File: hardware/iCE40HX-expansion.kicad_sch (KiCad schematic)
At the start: 32 parts, among them J1 EXT3, J2 EXT1, J3 AudioJack3_Ground, J4 Conn_01x34, J5 AudioJack3_Ground, J6 Conn_01x04, J8 DE15_Plug_HighDensity, U1 ADV7180BCP32Z-RL, U2 AMS1117-1.8, Y1 28.63636MHz

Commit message: finished component placement
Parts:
- added C24, C26: 0.1uf, Capacitor_SMD:C_0603_1608Metric, symbol Device:C_Small
- added C25, C27: 10uf, Capacitor_SMD:C_0805_2012Metric, symbol Device:C_Small
- added R56, R57: 270, Resistor_SMD:R_0603_1608Metric, symbol Device:R_Small
- added U5: 74LVC245A, Package_SO:TSSOP-20_4.4x6.5mm_P0.65mm, symbol New_Library:74LVC245A
- C22, C23: footprint Capacitor_SMD:C_0603_1608Metric -> Capacitor_SMD:C_0805_2012Metric
- J3, J5: value AudioJack3_Ground -> ~
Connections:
- net CLK is gone; now on net PIO1_20: J4.2 (Pin_2)
- net EN is gone; now on net PIO1_19: J4.4 (Pin_4)
- net HS is gone; now on net PIO0_20: U1.1 (HS)
- net INTRQ is gone; now on net PIO0_17: U1.32 (~{INTRQ})
- net LLC is gone; now on net PIO0_21: U1.11 (LLC)
- net SFL is gone; now on net PIO0_18: U1.4 (SFL)
- net VS is gone; now on net PIO0_19: U1.31 (VS/FIELD)
- net +1V8: now also U2.2 (VO), C24.1, C25.1
- net +3V3: now also U2.3 (VI), C26.1, C27.1, U5.1 (DIR), U5.19 (OE), U5.20 (VCC)
- net GND: now also U2.1 (GND), C24.2, C25.2, C26.2, C27.2, U5.10 (GND)
- net PIO0_00: no longer J4.29 (Pin_29)
- net PIO0_01: no longer J4.28 (Pin_28)
- net PIO0_02: no longer J4.27 (Pin_27)
- net PIO0_03: no longer J4.26 (Pin_26)
- net PIO0_04: no longer J4.25 (Pin_25)
- net PIO0_05: no longer J4.24 (Pin_24)
- net PIO0_06: no longer J4.23 (Pin_23)
- net PIO0_07: no longer J4.22 (Pin_22)
- net PIO0_08: no longer J4.21 (Pin_21)
- net PIO0_09: now also U1.16 (P0); no longer J4.20 (Pin_20)
- net PIO0_10: now also U1.15 (P1); no longer J4.19 (Pin_19)
- net PIO0_11: now also U1.10 (P2); no longer J4.18 (Pin_18)
- net PIO0_12: now also U1.9 (P3); no longer J4.17 (Pin_17)
- net PIO0_13: now also U1.8 (P4); no longer J4.16 (Pin_16)
- net PIO0_14: now also U1.7 (P5); no longer J4.15 (Pin_15)
- net PIO0_15: now also U1.6 (P6); no longer J4.14 (Pin_14)
- net PIO0_16: now also U1.5 (P7); no longer J4.13 (Pin_13)
- net PIO0_17: no longer J4.12 (Pin_12)
- net PIO0_18: no longer J4.11 (Pin_11)
- net PIO0_19: no longer J4.10 (Pin_10)
- net PIO0_20: no longer J4.9 (Pin_9)
- net PIO0_21: no longer J4.8 (Pin_8)
- net PIO0_22: no longer J4.7 (Pin_7)
- net PIO0_23: no longer J4.6 (Pin_6)
- net PIO1_14: no longer U1.16 (P0)
- net PIO1_15: no longer U1.15 (P1)
- net PIO1_16: no longer U1.10 (P2)
- net PIO1_17: no longer U1.9 (P3)
- net PIO1_18: no longer U1.8 (P4)
- net PIO1_19: no longer U1.7 (P5)
- net PIO1_20: no longer U1.6 (P6)
- net PIO1_21: now also J4.5 (Pin_5), U5.2 (A0); no longer U1.5 (P7)
- net PIO1_22: now also J4.3 (Pin_3), U5.3 (A1)
- net PIO1_23: now also J4.13 (Pin_13)
- net PIO1_24: now also J4.12 (Pin_12)
- net PIO1_25: now also J4.11 (Pin_11)
- net PIO1_26: now also J4.10 (Pin_10)
- net PIO1_27: now also J4.9 (Pin_9)
- net PIO1_28: now also J4.8 (Pin_8)
- net PIO1_29: now also J4.7 (Pin_7)
- net PIO1_30: now also J4.6 (Pin_6)
- net PIO1_31: now also J4.21 (Pin_21)
- net PIO1_32: now also J4.20 (Pin_20)
- net PIO1_33: now also J4.19 (Pin_19)
- net PIO1_34: now also J4.18 (Pin_18)
- net PIO1_35: now also J4.17 (Pin_17)
- net PIO1_36: now also J4.16 (Pin_16)
- net PIO1_37: now also J4.15 (Pin_15)
- net PIO1_38: now also J4.14 (Pin_14)
- net PIO1_39: now also J4.29 (Pin_29)
- net PIO1_40: now also J4.28 (Pin_28)
- net PIO1_41: now also J4.27 (Pin_27)
- net PIO1_42: now also J4.26 (Pin_26)
- net PIO1_43: now also J4.25 (Pin_25)
- net PIO1_44: now also J4.24 (Pin_24)
- net PIO1_45: now also J4.23 (Pin_23)
- net PIO1_46: now also J4.22 (Pin_22)
- net AIN1: no longer names the net of C4.1, U1.23 (AIN1)
- net AIN2: no longer names the net of C5.1
- net AIN2: now also U1.19 (AIN2); no longer U1.29 (AIN2)
- net HSYNC renamed VGA_HSYNC
- net VGA_HSYNC: now also R57.2; no longer J4.3 (Pin_3)
- net VSYNC renamed VGA_VSYNC
- net VGA_VSYNC: now also R56.2; no longer J4.5 (Pin_5)
- new net: R56.1, U5.18 (B0)
- new net: R57.1, U5.17 (B1)
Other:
- note added: "1V8 LDO"
- moved on the sheet: C1, C10, C11, C12, C13, C14, C15, C2, C22, C23, C3, C4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

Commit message: continuation
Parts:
- added C28: 0.1uf, Capacitor_SMD:C_0603_1608Metric, symbol Device:C_Small
- added C29: 10nf, Capacitor_SMD:C_0603_1608Metric, symbol Device:C_Small
- added D1, D2: LED, LED_SMD:LED_0805_2012Metric, symbol Device:LED
- added J7: Conn_02x10_Odd_Even, Connector_PinHeader_1.27mm:PinHeader_2x10_P1.27mm_Vertical_SMD, symbol Connector_Generic:Conn_02x10_Odd_Even
- added R58: 0, Resistor_SMD:R_1206_3216Metric, symbol Device:R
- added R59, R60, R61: 270, Resistor_SMD:R_0603_1608Metric, symbol Device:R_Small
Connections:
- net +1V8: now also R58.2; no longer C24.1, C25.1, U2.2 (VO)
- net +3V3: now also C28.1, C29.1, R59.2
- net +5V: now also R61.2
- net GND: now also U5.4 (A2), U5.5 (A3), U5.6 (A4), U5.7 (A5), U5.8 (A6), U5.9 (A7), C28.2, C29.2, D1.1 (K), D2.1 (K)
- net PIO0_00: now also J7.17 (Pin_17)
- net PIO0_01: now also J7.15 (Pin_15)
- net PIO0_02: now also J7.13 (Pin_13)
- net PIO0_03: now also J7.11 (Pin_11)
- net PIO0_04: now also J7.9 (Pin_9)
- net PIO0_05: now also J7.7 (Pin_7)
- net PIO0_06: now also J7.5 (Pin_5)
- net PIO0_07: now also J7.3 (Pin_3)
- net PIO0_08: now also J7.1 (Pin_1)
- net PIO0_23: now also J7.8 (Pin_8)
- net PIO0_24: now also J7.6 (Pin_6)
- net PIO0_25: now also J7.4 (Pin_4)
- net PIO0_26: now also J7.2 (Pin_2)
- net PIO0_27: now also J7.12 (Pin_12)
- net PIO0_28: now also J7.14 (Pin_14)
- net PIO0_29: now also J7.16 (Pin_16)
- net PIO0_30: now also J7.18 (Pin_18)
- net EXTCLK: no longer names the net of J1.6 (Pin_6)
- net EXTCLK: no longer J2.6 (Pin_6)
- new net: C24.1, C25.1, R58.1, U2.2 (VO)
- new net: D2.2 (A), R60.1
- new net: R60.2, R61.1
- new net: D1.2 (A), R59.1
- no-connect marks 9 -> 12
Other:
- note added: "INDICATOR"
- note added: "SYNC BUFFER"
- moved on the sheet: R56, R57, U5

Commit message: version 1.0
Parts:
- removed J3, J5: ~, Connector_Audio:Jack_3.5mm_KoreanHropartsElec_PJ-320D-4A_Horizontal, symbol Connector_Audio:AudioJack3_Ground
- added J3, J9: AudioJack4, Connector_Audio:Jack_3.5mm_KoreanHropartsElec_PJ-320D-4A_Horizontal, symbol Connector_Audio:AudioJack4
- U1: footprint C459884:LFCSP-32_L5.0-W5.0-P0.50-BL-EP3.6 -> Package_CSP:LFCSP-32-1EP_5x5mm_P0.5mm_EP3.6x3.6mm
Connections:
- net +3V3: no longer J2.3 (Pin_3), J2.5 (Pin_5)
- net +5V: no longer J2.1 (Pin_1)
- net GND: now also J3.S, J9.S
- net RST: now also J6.1 (Pin_1); no longer J6.3 (Pin_3)
- net SCLK: now also J6.3 (Pin_3); no longer J6.1 (Pin_1)
- net at R3.1: now also J3.T
- net at R2.1: now also J9.T
- no-connect marks 12 -> 15
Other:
- moved on the sheet: C5, R3, R4

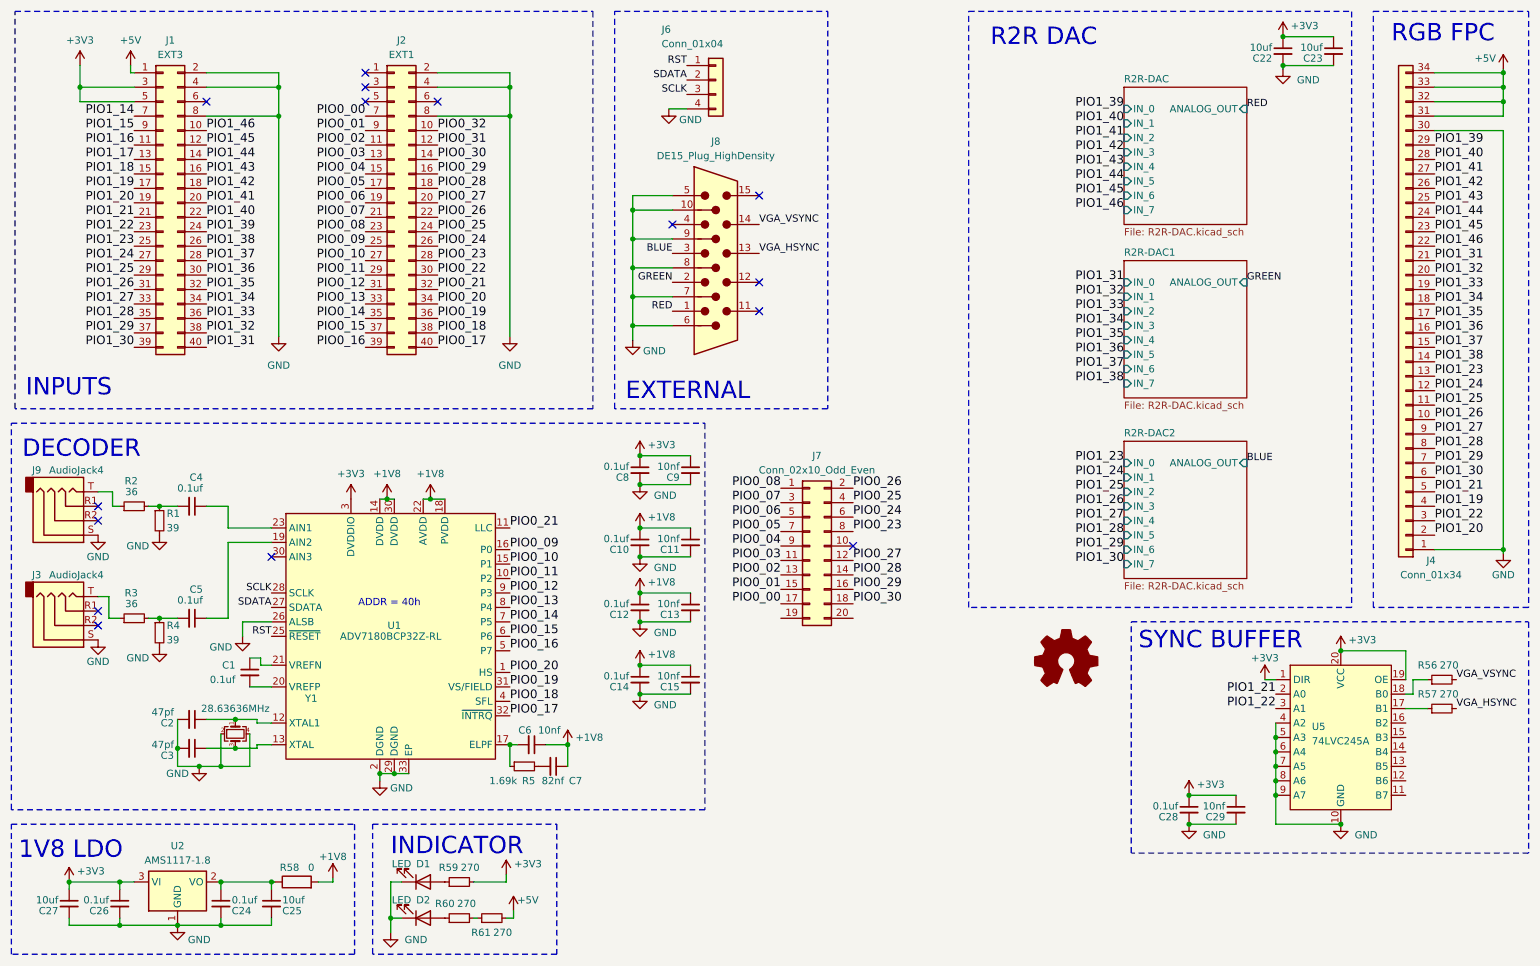
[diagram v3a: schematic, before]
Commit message: fixed error in sync buffer OE pin
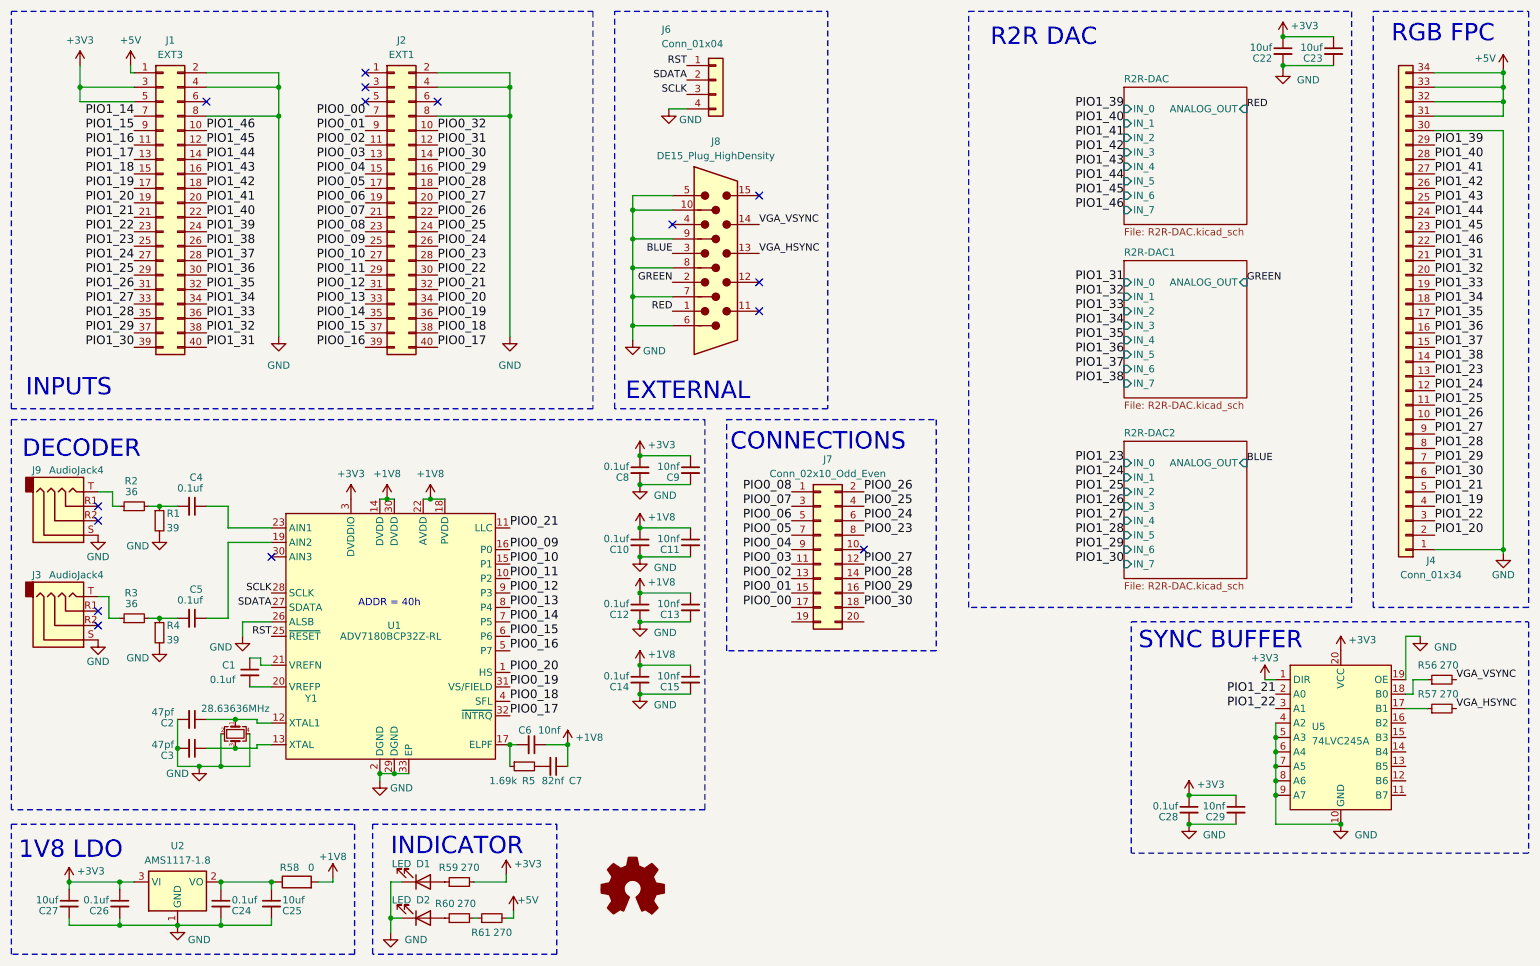
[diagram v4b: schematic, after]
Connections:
- net +3V3: no longer U5.19 (OE)
- net GND: now also U5.19 (OE)
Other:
- note added: "CONNECTIONS"
- moved on the sheet: J7
